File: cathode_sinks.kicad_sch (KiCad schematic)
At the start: 80 parts, among them Q10 BSS131, Q11 BSS131, Q12 BSS131, Q13 BSS131, Q14 BSS131, Q15 BSS131, Q16 BSS131, Q17 BSS131, Q18 BSS131, Q19 BSS131, Q20 BSS131, Q21 BSS131, Q22 BSS131, Q23 BSS131, Q24 BSS131, Q25 BSS131, Q26 BSS131, Q27 BSS131, Q28 BSS131, Q29 BSS131, Q30 BSS131, Q31 BSS131, Q32 BSS131, Q33 BSS131, Q34 BSS131, Q35 BSS131, Q36 BSS131, Q37 BSS131, Q38 BSS131, Q39 BSS131, Q40 BSS131, Q41 BSS131, Q42 BSS131, Q43 BSS131, Q44 BSS131, Q45 BSS131, Q46 BSS131, Q47 BSS131, Q48 BSS131, Q9 BSS131

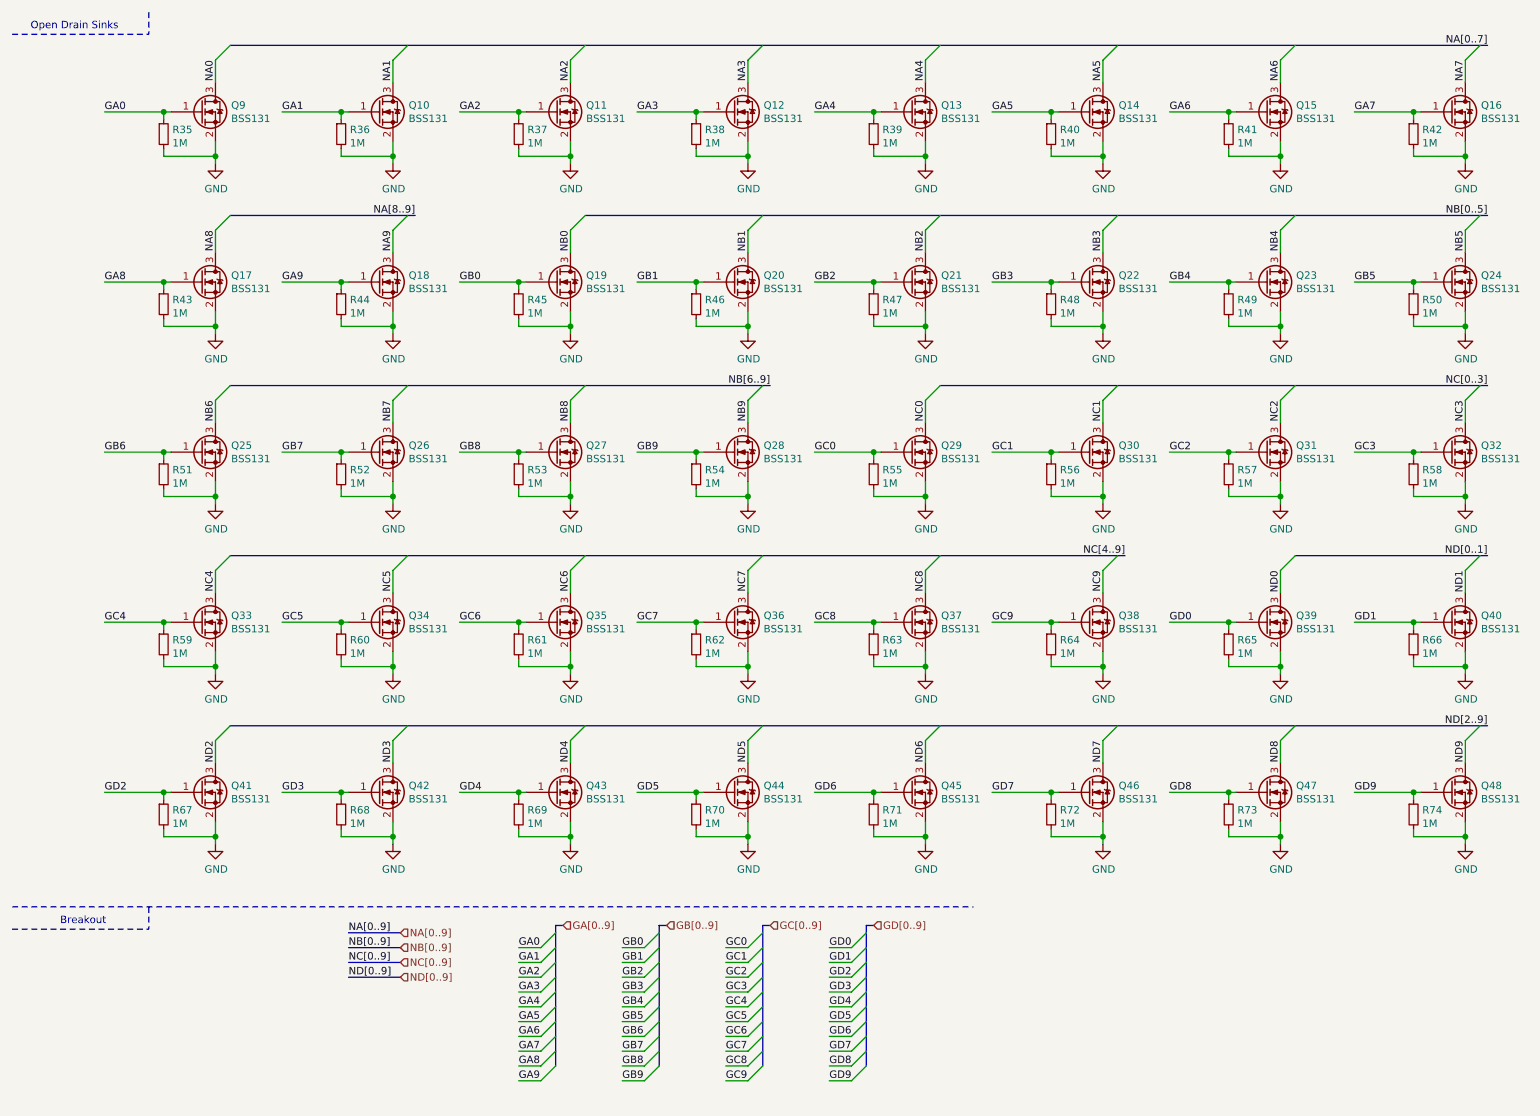
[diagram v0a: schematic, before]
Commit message: added outputs for schematic and gerber view
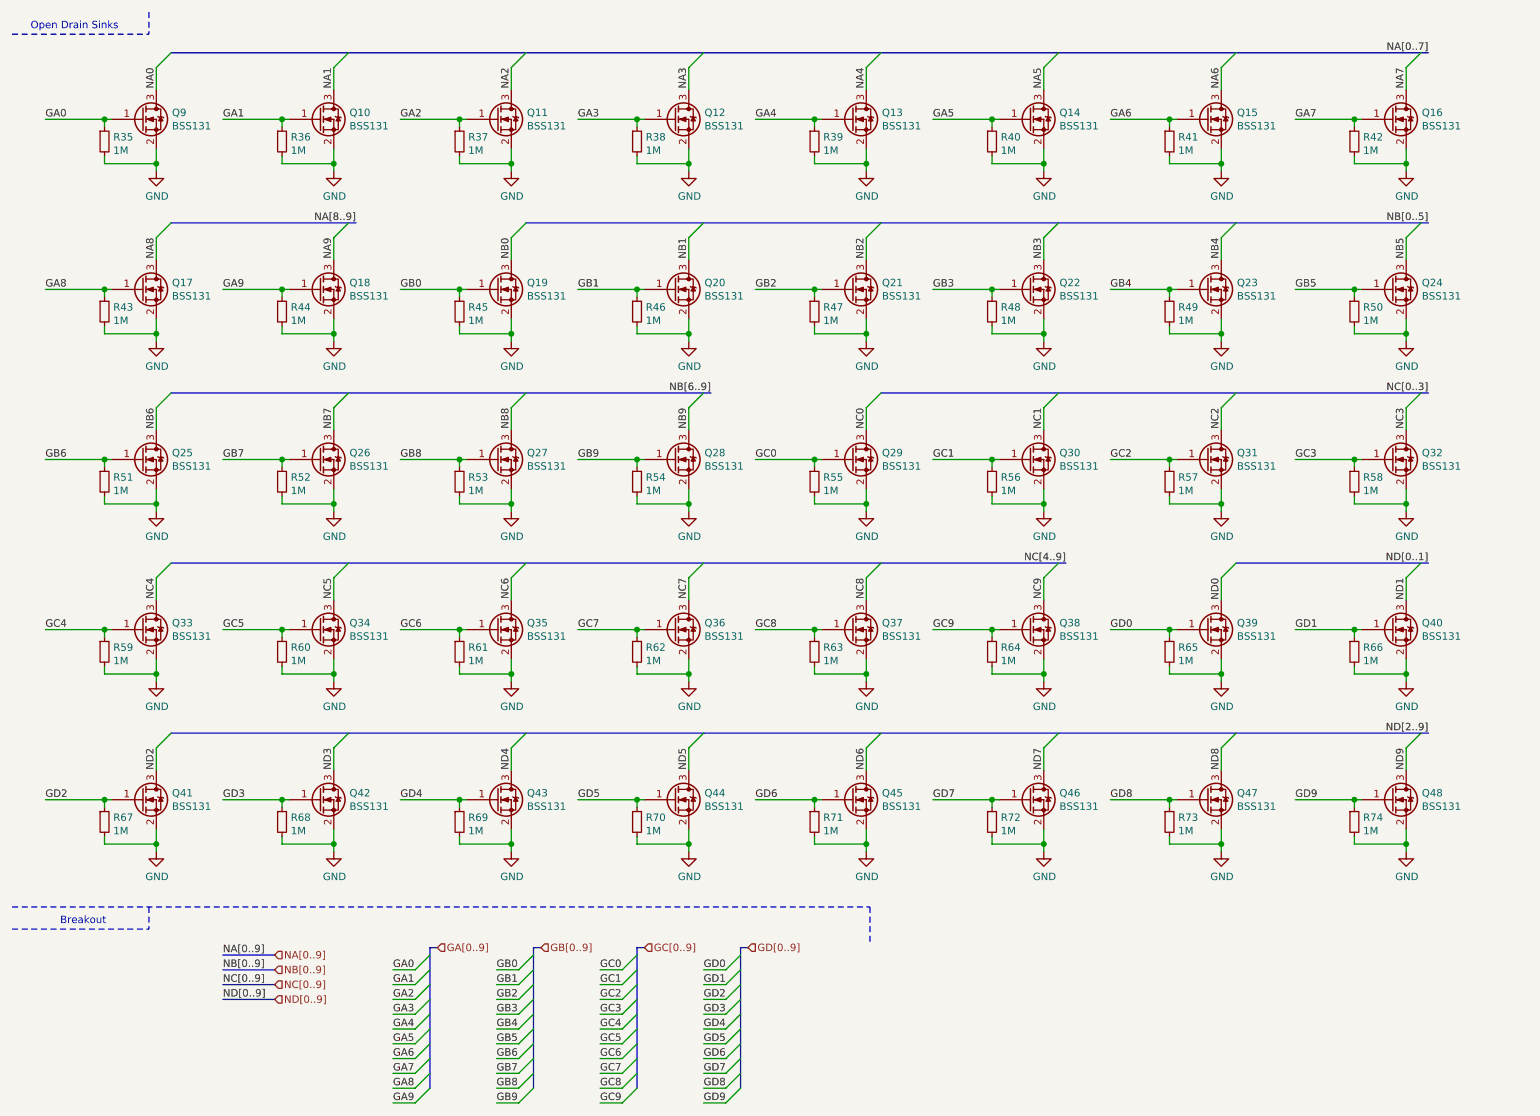
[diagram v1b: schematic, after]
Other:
- moved on the sheet: Q10, Q11, Q12, Q13, Q14, Q15, Q16, Q17, Q18, Q19, Q20, Q21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
